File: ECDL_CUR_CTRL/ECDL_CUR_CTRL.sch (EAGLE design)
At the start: 91 parts, among them IC1 LM317MDT, IC2 LM399H, IC3 OPA2227D, Q1 IRF9Z14, U1 INA213AIDCKT, U2 AD8671ARZ, U3 DMG3415U-7

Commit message: Added analog temperature controller.
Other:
- note added: "Author: Alexander Impertro"
- note added: "Revision 1.0"
- moved on the sheet: C1, C12, C13, C14, C15, C16, C17, C18, C19, C2, C20, C21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

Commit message: Preliminary changes to new version.
New features: Microntroller for current driver as well, seperate A/D
grounding, upgrade to ARM Cortec uC, several other improvements.
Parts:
- removed RS: 0.02R, adafruit:R-US_M1206
- removed T2, T4: (no value), transistor:MMBT3904LT1-NPN-SOT23-BEC
- removed T3: (no value), transistor:MMBT3906LT1-PNP-SOT23-BEC
- removed U2: AD8671ARZ, Analog Devices_By_element14_Batch_1:AD8671ARZ
- added C30, C33, C34, C36, C37, C39, C47, C48, C57: 10uF, rcl:C-EUC0805
- added C31, C32, C38, C40, C41, C44, C45, C46, C49, C50, C51, C52, C54, C55, C56, C58: 100nF, rcl:C-EUC0805
- added C35: 10nF, rcl:C-EUC0805
- added C42, C43: 0.1uF, rcl:C-EUC0805
- added C53: 1uF, rcl:C-EUC0805
- added CN1: (no value), adafruit:USBMINIB
- added D4: 3A/40V/500mV, SparkFun-DiscreteSemi:DIODE-SCHOTTKY-B340A
- added F1: MF-MSMF050-2 500mA, Arduino-M0-V1:PROTEZIONE_0002_MF-MSMF050-2
- added IC10: 74LVC1G125DCKR, Arduino-M0-V1:INTEGRATEDCIRCUITS_0040_SN74LVC1G125DCKR
- added IC5: LM340S-12, linear:LM340S-12
- added IC6: L7912, misc-ics:L7912
- added IC7, IC9: AD8676, analog-devices:AD8656R
- added IC8: TL071D, linear:TL071D
- added JP6: (no value), pinhead:PINHD-2X3
- added JP7: (no value), pinhead:PINHD-1X5
- added L4: MH2029-300Y, Arduino-M0-V1:PROTEZIONE_0001_BLM21PG300SN1D_/_MH2029-300Y
- added Q2: 2N7002, Seeed-Transistor:SMD-MOSFET-N-CH-60V-300MA-LOGIC-LEVEL-FET-2N7002(SOT-23)
- added Q3: SSM3J328R,LF, Seeed-Transistor:SMD-MOSFET-P-CH-20V-6A-SSM3J328R(SOT-23)
- added R24, R47, R60, R61, R62: 100K, rcl:R-US_R0805
- added R33, R34, R35, R36, R37, R38, R39, R40, R41, R42, R43, R44, R45, R46, R48, R49, R50, R51, R52, R53, R54, R55, R57, R58, R59, R64, R65, R66, R67: 10K, rcl:R-US_R0805
- added R56, R63: 330R, rcl:R-US_R0805
- added RMON: 50R, rcl:R-US_R0805
- added S1: MOM SWITCH, SparkFun-Switches:MOMENTARY-SWITCH-SPST-SMD-5.2MM
- added TP3, TP4: TEST-POINT2, SparkFun-Connectors:TEST-POINT2
- added TR1: PMV48XP, Arduino-M0-V1:TRANSISTORS_0297_PMV48XP
- added U4: TS514AID, ST Microelctronics_By_element14_Batch_1:TS514AID
- added U5: LM1117IMP-3.3, NSC_By_element14_Batch_1.1:LM1117IMP-3.3
- added U6: LM1117IMP-5.0, NSC_By_element14_Batch_1.1:LM1117IMP-5.0
- added X3: (no value), adafruit:SMACONNECTOR
- added Y1: 32,768Khz_SMD, Arduino-M0-V1:CRISTALLI_0213_ABS07-32.768KHZ-T
- added Z1, Z2: BRNCG0603MLC-05E, Arduino-M0-V1:PROTEZIONE_0010_BRNCG0603MLC-05E
- C1: value 100nF -> 10nF; device rcl:C-EUC0603 -> rcl:C-EUC0805
- C11: value C_SNUB -> Cfb; device rcl:C-EUC0603 -> rcl:C-EUC0805
- C12: value 1u -> 1uF; device rcl:C-EUC0603 -> rcl:C-EUC0805
- C13, C14, C15, C16, C17, C2, C20, C21, C25, C28, C7, C8: device rcl:C-EUC0603 -> rcl:C-EUC0805
- C18, C19, C22, C26, C29: value 0.1uF -> 100nF; device rcl:C-EUC0603 -> rcl:C-EUC0805
- C23: value 10uF -> 10nF; device rcl:C-EUC0603 -> rcl:C-EUC0805
- C24: value 0.1uF -> 10uF; device rcl:C-EUC0603 -> rcl:C-EUC0805
- C27: value 10uF -> 100nF; device rcl:C-EUC0603 -> rcl:C-EUC0805
- JP3: device pinhead:PINHD-1X3 -> pinhead:PINHD-2X4
- R1, R10, R12, R13, R14, R15, R16, R17, R18, R19, R2, R20, R21, R22, R5, R6, R8: device rcl:R-US_R0603 -> rcl:R-US_R0805
- R23, R25, R26, R29: value 470K -> 10K; device rcl:R-US_R0603 -> rcl:R-US_R0805
- R27: value 10K -> 28.7K; device rcl:R-US_R0603 -> rcl:R-US_R0805
- R28: value 1K -> 11K; device rcl:R-US_R0603 -> rcl:R-US_R0805
- R30: value 100K -> 10K; device rcl:R-US_R0603 -> rcl:R-US_R0805
- R31: value 1M -> 10K; device rcl:R-US_R0603 -> rcl:R-US_R0805
- R32: value 1K -> 10K; device rcl:R-US_R0603 -> rcl:R-US_R0805
- R4: value 50 -> 50R; device rcl:R-US_R0603 -> rcl:R-US_R0805
- R7: value 10K -> 1K; device ecdl_parts:BOURNS3590 -> rcl:R-US_R0805
- R9: value R_SNUB -> 100R; device rcl:R-US_R0603 -> rcl:R-US_R0805
- U1: value INA213AIDCKT -> ATSAMD21G-A; device Texas Instruments_By_element14_Batch_1:INA213AIDCKT -> SparkFun-IC-Microcontroller:ATSAMD21G-A
- U3: value DMG3415U-7 -> AD5541; device Diodes_Inc_By_element14_Batch_1:DMG3415U-7 -> misc-ics:AD5541
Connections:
- removed net N$31: R26.1, R27.1, T3.C
- removed net N$4 (its old number): C17.2, IC3A.+IN, L3.2, R15.1, R16.1, RS.1, U1.IN+
- removed net N$6 (its old number): R6.2, R7.S
- new net +12V: C19.1, C20.1, C24.1, C26.1, C33.1, C40.1, C42.1, C47.1, C49.1, C57.1, C58.2, IC2.3, IC3P.V+, IC5.VO, IC7P.V+, IC8.V+, IC9P.V+, Q3.S, R23.2, R60.2, TP3.1, U4.VCC+, U6.VIN
- new net +3V3: C18.1, C37.1, C51.1, C52.1, IC10P.VDD, JP3.1, JP3.2, L4.2, R30.2, R57.2, R58.2, R62.2, U1.VDDIN, U1.VDDIO@17, U1.VDDIO@36, U5.VOUT, U5.VOUT_2
- new net +5V: C34.1, C46.1, JP6.2, JP7.1, R44.2, R45.2, TR1.S, U5.VIN, U6.VOUT, U6.VOUT_2
- new net -12V: C21.1, C22.1, C25.2, C27.2, C38.2, C39.2, C41.1, C48.2, C50.2, IC2.4, IC3P.V-, IC6.VO, IC7P.V-, IC8.V-, IC9P.V-, R8.2, TP4.1, U4.VCC-
- new net CS: R41.1
- new net DACGND: C30.2, C31.2, C32.2, IC7A.IN-, IC7A.OUT, R36.2, R37.2, R38.2, U3.AGND, U3.DGND
- new net DCLK: R29.1, U3.CLK, U4.OUT1
- new net DCS: R52.1, U3.CS, U4.OUT4
- new net DCURMON: R32.1, U4.OUT3
- new net DDATA: R31.1, U3.DATA, U4.OUT2
- new net DGND: C18.2, C23.2, C33.2, C34.2, C35.2, C36.1, C37.2, C44.2, C45.2, C51.2, C52.2, C53.2, C54.2, C55.1, C56.1, CN1.GND, IC10P.VSS, JP3.3, JP3.4, JP6.6, JP7.3, R34.2, R35.2, R47.1, R53.2, R54.2, R59.1, R61.1, R65.2, S1.1, U1.GND@18, U1.GND@35, U1.GND@42, U1.GNDANA, U5.ADJ/GND, U6.ADJ/GND, Z1.2, Z2.2
- new net ENCA: C45.1, R43.1, U1.PA09(I2C/AIN17/SER0:1+)
- new net ENCB: C44.1, R42.1, U1.PA08(I2C/AIN16/SER0:0+)
- new net ENCBTN: C46.2, R46.1, U1.PA10(AIN18/SER0:2+)
- new net MOSI: R40.1
- new net N$29: IC7A.IN+, R27.2, R28.1
- new net N$35: C17.1, IC3A.+IN, JP4.1, L3.2, R15.2, R16.1
- new net N$36: JP7.2, R42.2, R45.1
- new net N$38: IC8.+IN, R64.2, R65.1
- new net N$39: R32.2, R33.1, U4.NEG3
- new net N$40: JP7.4, R43.2, R44.1
- new net N$41: R37.1, R40.2, U4.POS2
- new net N$42: R38.1, R41.2, U4.POS4
- new net N$43: JP7.5, R46.2, R47.2
- new net N$44: C55.2, U1.PA00(XIN32/SER1:0/TC2:0), Y1.2
- new net N$45: C56.2, U1.PA01(XOUT32/SER1:1/TC2:1), Y1.1
- new net N$46: IC10A.O, R60.1, R61.2, TR1.G
- new net N$47: IC8.-IN, R66.2, R67.1
- new net N$5: R5.1, U3.VOUT
- new net N$50: IC9A.IN-, IC9A.OUT, R49.2
- new net N$51: IC9B.IN+, R48.1, R51.2
- new net N$52: IC9B.IN-, R49.1, R50.2
- new net N$54: IC9B.OUT, R50.1, RMON.2
- new net N$55: R54.1, R55.2, U4.POS3
- new net N$56: R52.2, R53.1, U4.NEG4
- new net N$9: IC7B.OUT, R10.2
- new net PA02_AIN0: U1.PA02(AIN0/DAC)
- new net PA04_AIN4: U1.PA04(AIN4/REFB/SER0:0/TC0:0)
- new net PA05_AIN5: U1.PA05(AIN5/SER0:1/TC0:1)
- new net PA28_USB_HOST_EN: R63.1, U1.PA28
- new net PB02_AIN10: U1.PB02(AIN10/SER5:0)
- new net PB08_AIN2: U1.PB08(AIN2/SER4:0/TC4:0)
- new net PB09_AIN3: U1.PB09(AIN3/SER4:1/TC4:1)
- new net PB10_S4_SPI_MOSI: JP6.4, U1.PB10(SER4:2+)
- new net PB11_S4_SPI_SCK: JP6.3, U1.PB11(SER4:3+)
- new net PB12_S4_SPI_MISO: JP6.1, U1.PA12(I2C/SER2:0+)
- new net RESET: JP6.5, R30.1, R56.1, S1.2
- new net SCK: R39.1
- new net SCL: JP3.7, JP3.8, R58.1, U1.PA23(I2C/SER3:0+)
- new net SDA: JP3.5, JP3.6, R57.1, U1.PA22(I2C/SER3:0+)
- new net TARGET_RESET: C23.1, R56.2, U1.!RESET!
- new net TARGET_USB_N: CN1.D-, U1.PA24(SER3:2+), Z1.1
- new net TARGET_USB_P: CN1.D+, U1.PA25(SER3:3+), Z2.1
- new net USBVCC: C36.2, F1.2, R59.2, TR1.D
- new net USB_ID: CN1.ID, IC10A.I, IC10A.OE, R62.1, R63.2
- new net VDDCORE: C53.1, U1.VDDCORE
- new net VIN: IC8.OUT, R67.2
- new net VMON: R55.1, RMON.1
- new net XUSB: C35.1, CN1.VBUS, F1.1
- net GND: now also C19.2, C20.2, C25.1, C27.1, C38.1, C39.1, C40.2, C41.2, C43.2, C47.2, C48.1, C49.2, C50.1, C57.2, C58.1, IC5.GND, IC6.GND, Q2.S, R12.1, R20.1, R26.1, R33.2, R4.2, R51.1; no longer C18.2, C19.1, C20.1, C23.2, C25.2, C27.2, JP3.3, R12.2, R20.2, R29.2, R4.1, T2.E, T4.E, U1.GND, U1.REF
- net N$1: now also R1.2, R2.2; no longer R1.1, R2.1
- net N$10: now also R29.2, R35.1, U4.NEG1; no longer R10.2, U2.OUT
- net N$12: now also C43.1, Q2.G, R25.1; no longer R28.1
- net N$13: now also IC7B.IN-, IC9A.IN+; no longer U2.-IN
- net N$15: now also R12.2; no longer R12.1
- net N$16: now also R15.1; no longer R15.2
- net N$17: now also R17.2; no longer R17.1
- net N$18: now also R17.1, R4.1; no longer R17.2, R4.2
- net N$20: now also C17.2, R20.2; no longer C17.1, R20.1
- net N$23: now also R36.1, R39.2, U4.POS1; no longer JP4.1, RS.2, U1.IN-
- net N$24: now also D4.C, R7.2; no longer R32.2, U3.D
- net N$25: now also C54.1, L4.1, U1.VDDANA; no longer JP3.2, U1.OUT
- net N$26: now also C28.1, JP1.2, R24.1; no longer R23.1, R25.2, T2.C
- net N$27: now also R1.1; no longer R1.2
- net N$28: now also C42.2, Q2.D, Q3.G, R23.1, R24.2; no longer C28.1, JP1.2, R25.1
- net N$3: now also R2.1; no longer R2.2
- net N$30: now also D4.A, Q3.D, R25.2; no longer T2.B
- net N$32: now also R31.2, R34.1, U4.NEG2; no longer R27.2, R28.2, R29.1, T4.B
- net N$33: now also R66.1, X3.GND1, X3.GND2, X3.GND3, X3.GND4; no longer R30.2, T4.C, U3.G
- net N$34: now also R64.1, X3.ANT; no longer R30.1, R31.2, T3.B
- net N$37: now also R7.1; no longer R32.1
- net N$7: now also IC7B.IN+, R6.2; no longer R5.1, U2.+IN
- net N$8: now also R28.2; no longer R7.A
- net V+: now also IC5.VI; no longer C18.1, C19.2, C20.2, C23.1, C26.1, C27.1, IC2.3, IC3P.V+, JP3.1, R23.2, R31.1, T3.E, U1.V+, U2.V+, U3.S
- net V-: now also IC6.VI; no longer C21.1, C22.1, C24.1, C25.1, IC2.4, IC3P.V-, R8.2, U2.V-
- net VCCINT: now also C30.1, C31.1, C32.1, R27.1, R48.2, U3.REF, U3.VDD; no longer R7.E
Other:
- note added: "+5V"
- note added: "A"
- note added: "B"
- note added: "BTN"
- note added: "CS"
- note added: "DACGND"
- note added: "DCLK"
- note added: "DCS"
- note added: "DCURMON"
- note added: "DDATA"
- note added: "GND"
- note added: "INPUT FILTERING AND +/-12 V REGULATION"
- note added: "LD VOLTAGE REGULATION"
- note added: "MOSFET SOFT LATCH"
- note added: "MOSI"
- note added: "ROTARY ENCODER"
- note added: "SCK"
- note added: "VMON"
- note removed: "PANEL METER"

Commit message: Rev1.1 of CUR CTRL Complete, Ready for Mfg. Temp Ctrl WIP
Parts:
- removed LED1: (no value), led:LEDCHIPLED_0805
- added JP10, JP12: (no value), pinhead:PINHD-1X3
- added JP11, JP8, JP9: (no value), pinhead:PINHD-1X2
- added R68, R69, R70: 0R, rcl:R-US_R0805
- added V+: (no value), led:LEDCHIPLED_0805
- C11: value Cfb -> 33nF
- RMON: value 50R -> 50R or 0R
- renumbered CN1 to USB, LED2 to V-
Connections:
- net PB08_AIN2 renamed N$31
- removed net CS: R41.1
- removed net MOSI: R40.1
- removed net PB02_AIN10: U1.PB02(AIN10/SER5:0)
- removed net PB09_AIN3: U1.PB09(AIN3/SER4:1/TC4:1)
- removed net SCK: R39.1
- new net CS_DAC: R41.1, U1.PA15(XOUT/SER2:3+)
- new net MOSI_DAC: R40.1, U1.PA13(I2C/SER2:1+)
- new net N$48: JP10.3, U1.PA21(SER5:3+)
- new net N$49: JP10.2, U1.PA20(SER5:2+)
- new net N$53: JP10.1, U1.PA19(SER1:3+)
- new net SCK_DAC: R39.1, U1.PA14(XIN/SER2:2+)
- net +12V: now also JP12.3
- net +3V3: now also JP11.1
- net +5V: now also JP9.1
- net DCURMON: now also U1.PB09(AIN3/SER4:1/TC4:1)
- net DGND: now also JP11.2, JP9.2, R68.2, R69.2, R70.2
- net GND: now also JP12.2, R68.1, R69.1, R70.1, V+.C; no longer LED1.C
- net N$21: now also V+.A; no longer LED1.A
- net PA04_AIN4: now also JP8.2
- net PA05_AIN5: now also JP8.1
- net V+: now also JP12.1
- net VIN: now also U1.PB02(AIN10/SER5:0)
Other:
- note added: "ANALOG INPUT"
- note added: "CURRENT MONITOR"
- note added: "FAST AC-COUPLED MOD INPUT"
- note added: "OP-AMP BUFFERED MOD INPUT"
- note added: "Revision 1.1"
- note removed: "CS"
- note removed: "MOSI"
- note removed: "Revision 1.0"
- note removed: "SCK"
- moved on the sheet: C12, C17, C19, C20, C21, C22, C38, C39, C57, C58, IC3A, IC3B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

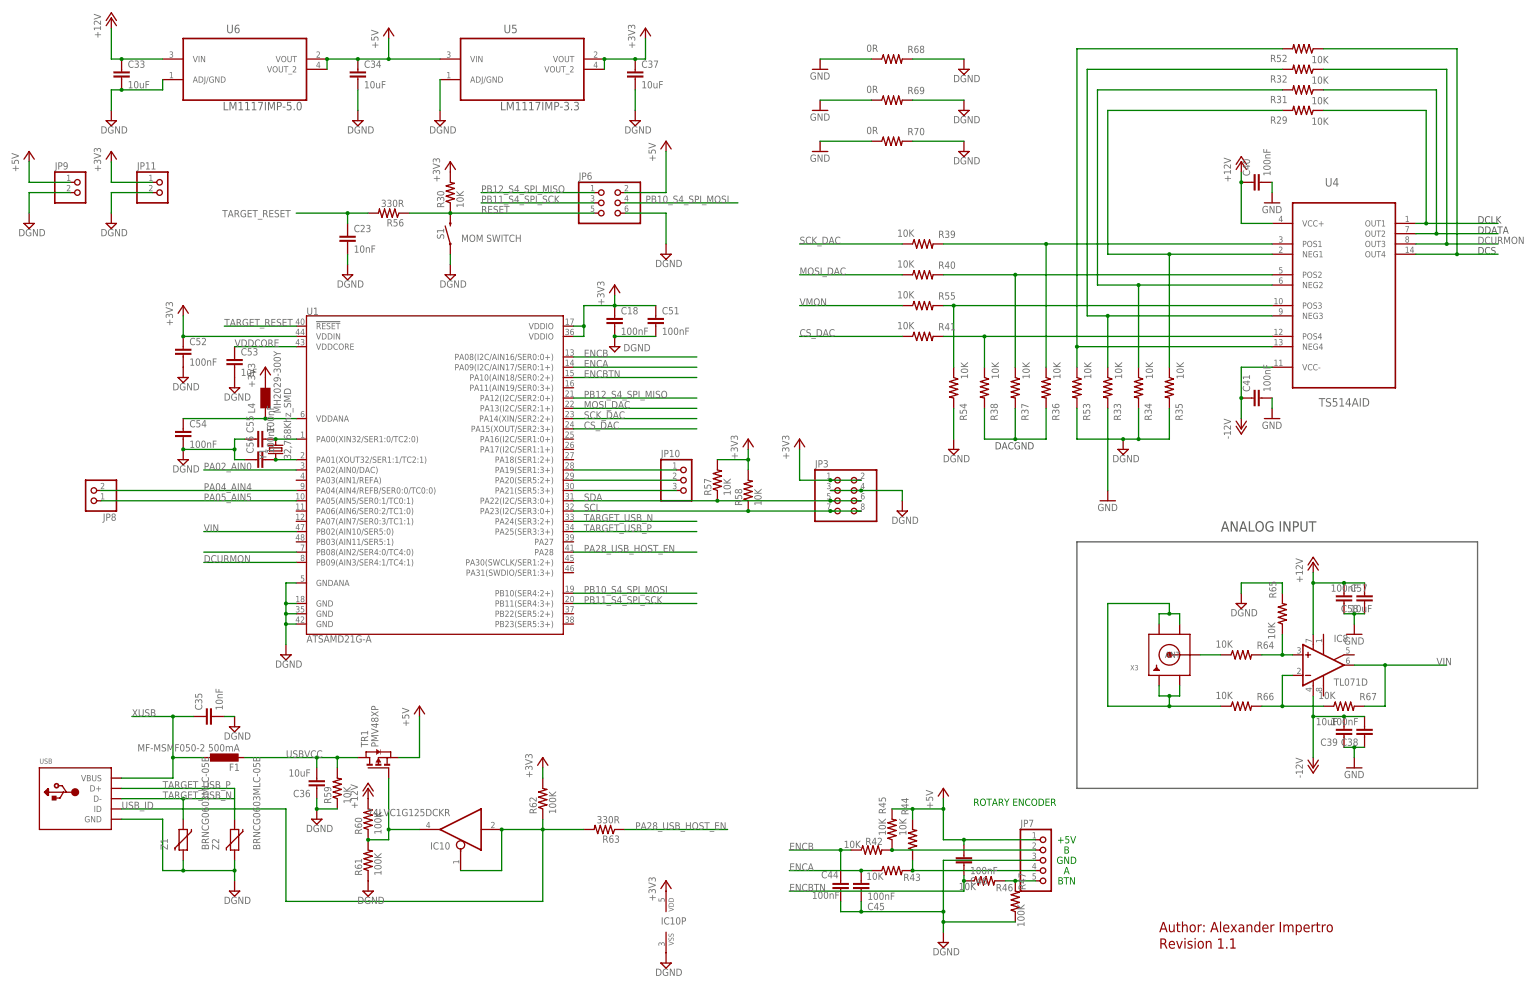
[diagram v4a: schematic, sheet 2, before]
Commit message: Changes to Analog PID. Added LTC1923 Design.
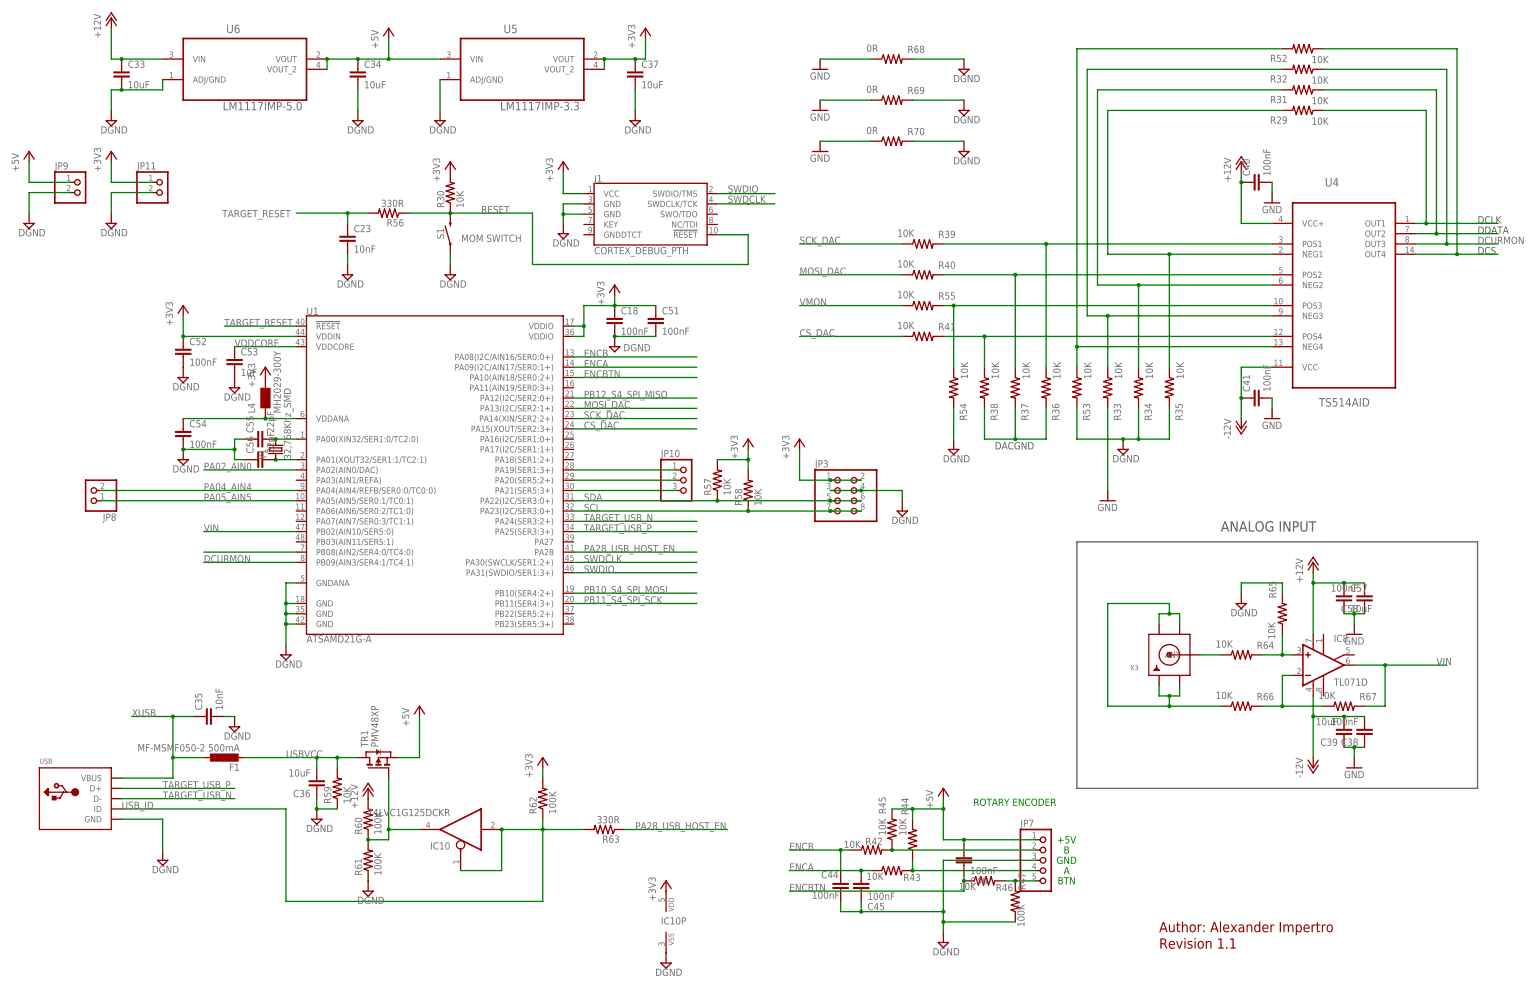
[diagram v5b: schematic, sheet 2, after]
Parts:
- removed JP6: (no value), pinhead:PINHD-2X3
- removed Z1, Z2: BRNCG0603MLC-05E, Arduino-M0-V1:PROTEZIONE_0010_BRNCG0603MLC-05E
- added J1: CORTEX_DEBUG_PTH, SparkFun-Connectors:CORTEX_DEBUG_PTH
- C55, C56: value 100nF -> 22pF
- T1: value (none) -> MMBT2907
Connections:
- new net SWDCLK: J1.SWDCLK/TCK, U1.PA30(SWCLK/SER1:2+)
- new net SWDIO: J1.SWDIO/TMS, U1.PA31(SWDIO/SER1:3+)
- net +3V3: now also J1.VCC
- net +5V: no longer JP6.2
- net DGND: now also J1.GND@3, J1.GND@5; no longer JP6.6, Z1.2, Z2.2
- net PB10_S4_SPI_MOSI: no longer JP6.4
- net PB11_S4_SPI_SCK: no longer JP6.3
- net PB12_S4_SPI_MISO: no longer JP6.1
- net RESET: now also J1.!RESET; no longer JP6.5
- net TARGET_USB_N: no longer Z1.1
- net TARGET_USB_P: no longer Z2.1
